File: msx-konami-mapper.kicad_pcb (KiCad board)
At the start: 2 copper layers, 65.3 x 63 mm, 1 part

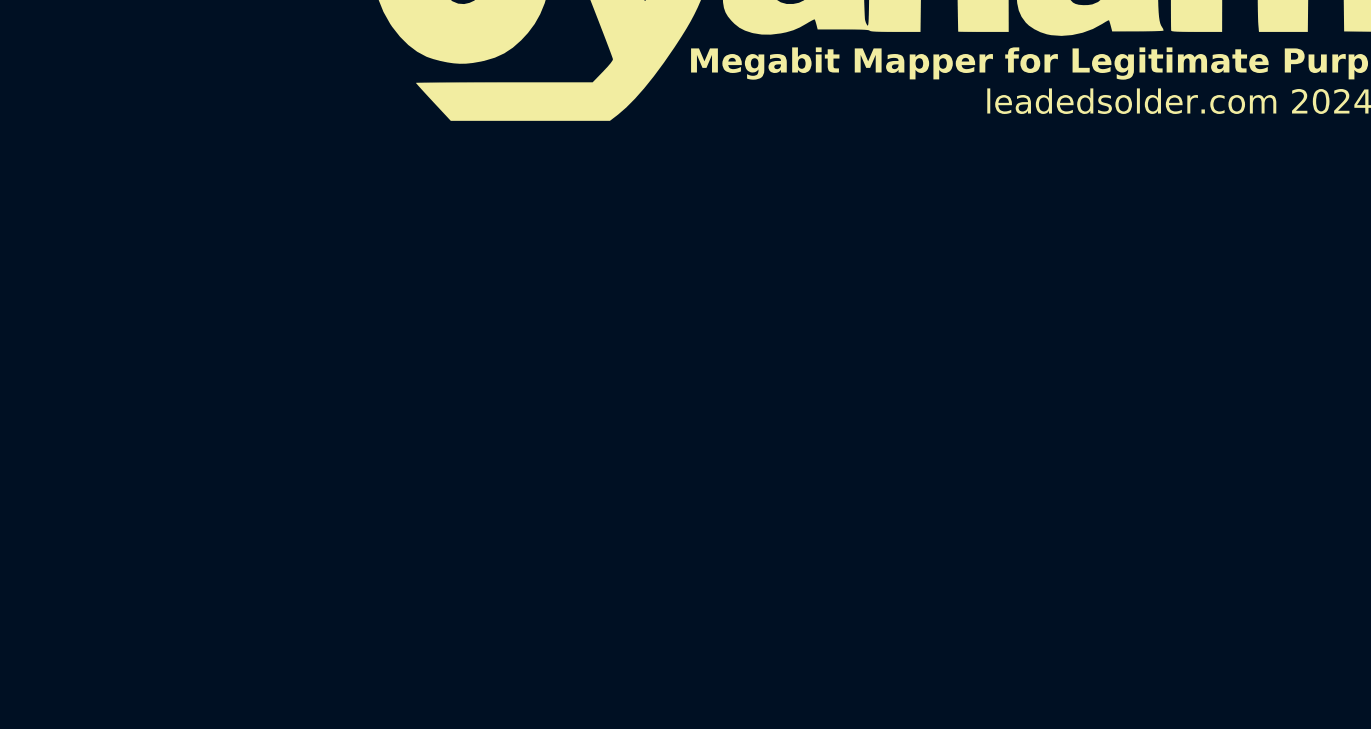
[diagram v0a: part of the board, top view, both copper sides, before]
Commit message: Placed EPROM, I may regret this
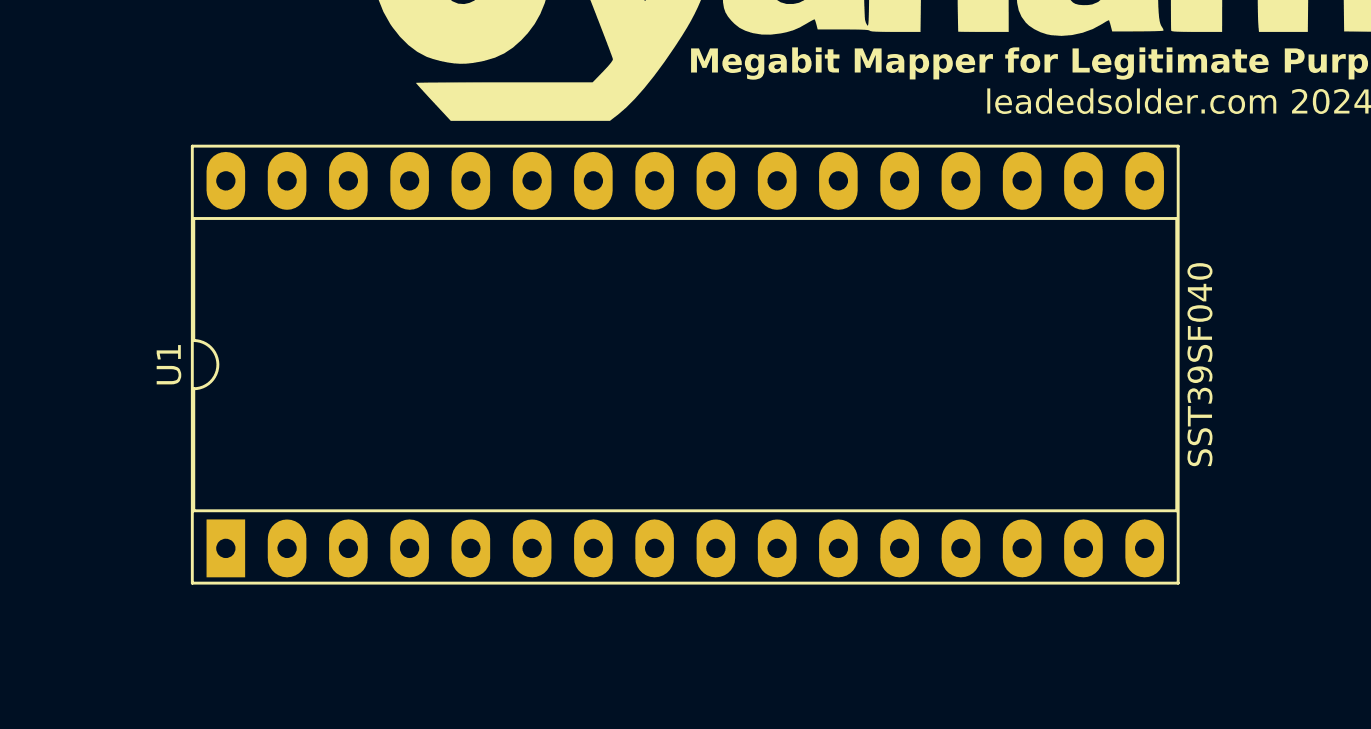
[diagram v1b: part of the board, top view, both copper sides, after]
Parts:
- added U1: SST39SF040, Package_DIP:DIP-32_W15.24mm_Socket_LongPads, F.Cu at (153.7, 80.0)

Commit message: Edge connector
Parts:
- added U2: ~, MSX:Cartridge, F.Cu at (142.2, 100.3)

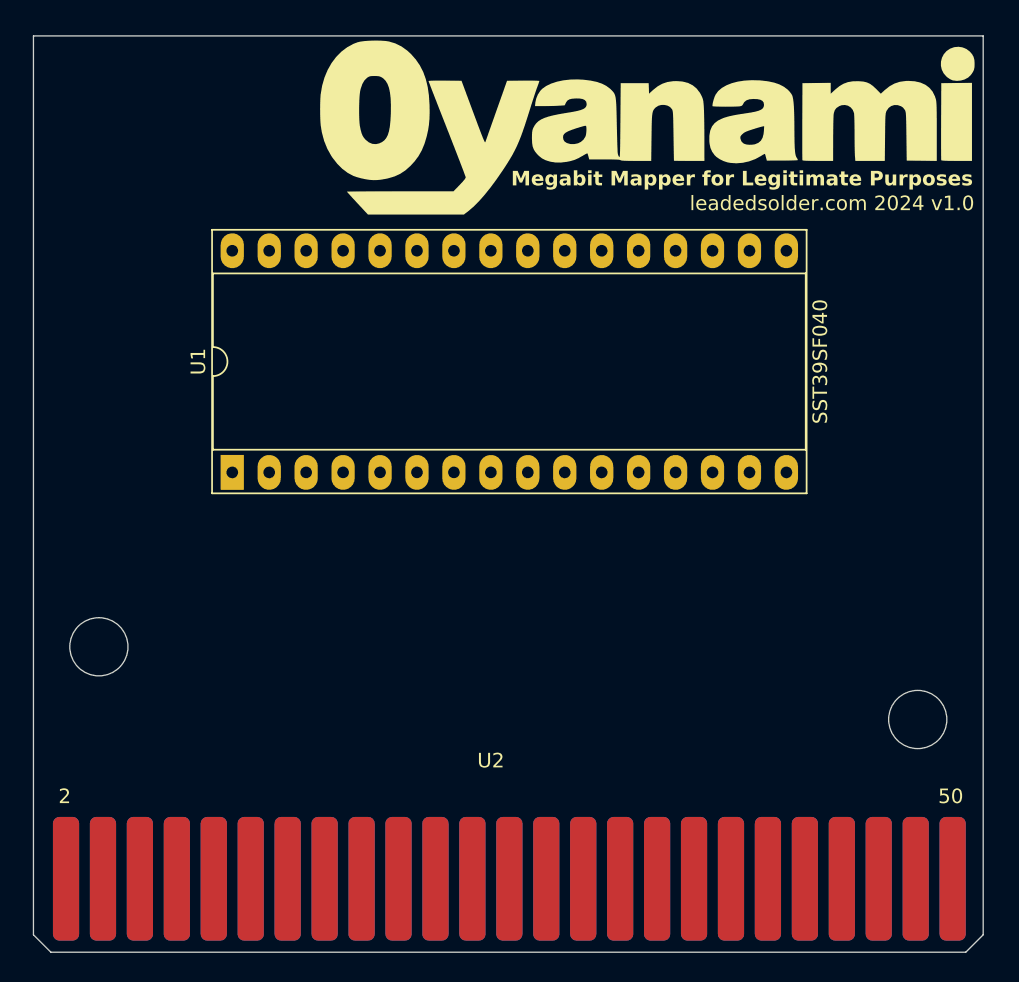
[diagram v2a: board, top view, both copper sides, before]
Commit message: Put the connector the right way around, dimwit
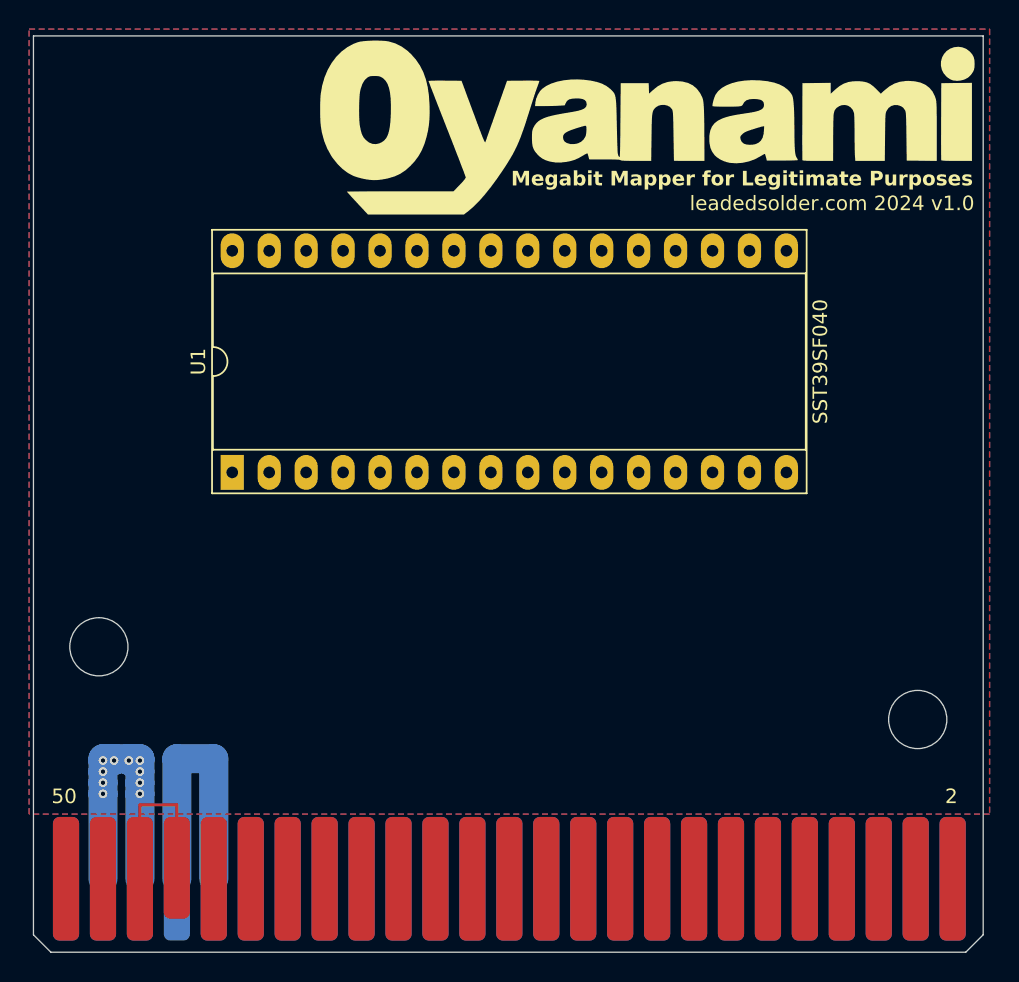
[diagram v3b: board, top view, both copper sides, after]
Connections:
- U2 pad 44: unconnected-(U2-SW1-Pad44) -> Net-(U2-SW1)
- U2 pad 46: unconnected-(U2-SW2-Pad46) -> Net-(U2-SW1)
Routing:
- net +5V: track 0.00 -> 19.3 mm, vias 0 -> 10
- net GND: track 0.00 -> 19.1 mm
- net Net-(U2-SW1): track 0.00 -> 12.0 mm
- added copper zone on F.Cu, net +5V
- added copper zone on B.Cu, net GND

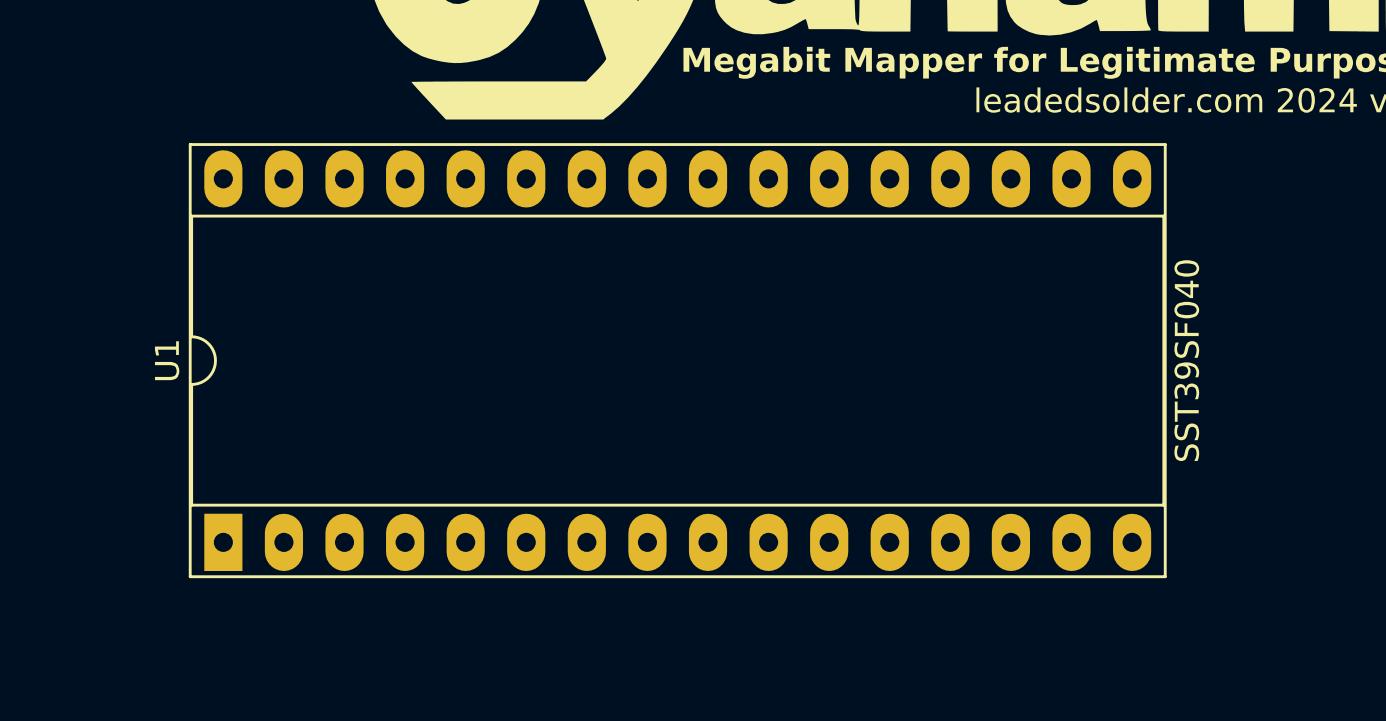
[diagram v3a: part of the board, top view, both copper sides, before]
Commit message: Data pins
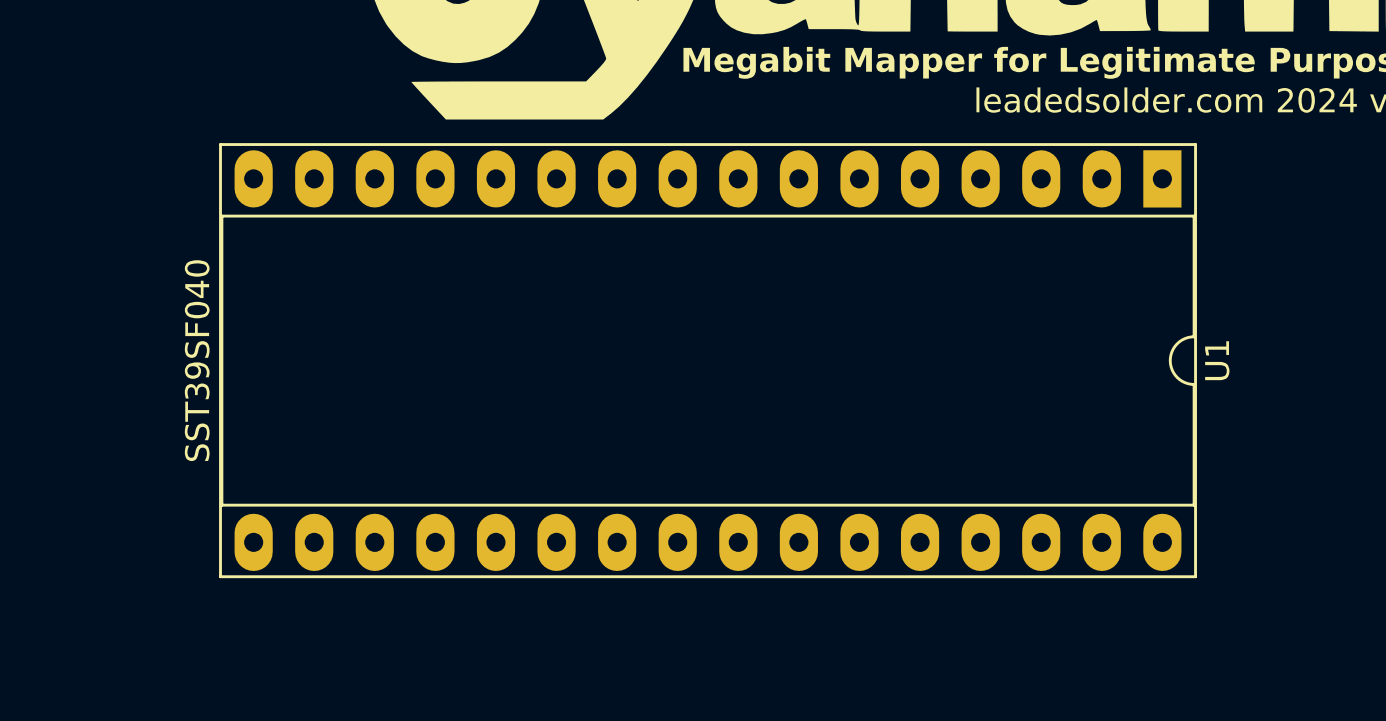
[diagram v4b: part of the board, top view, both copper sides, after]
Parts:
- moved U1 42.2 mm to (193.0, 64.8), turned to -90 degrees
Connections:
- U1 pad 13: unconnected-(U1-D0-Pad13) -> /D0
- U1 pad 14: unconnected-(U1-D1-Pad14) -> /D1
- U1 pad 15: unconnected-(U1-D2-Pad15) -> /D2
- U1 pad 16: unconnected-(U1-GND-Pad16) -> GND
- U1 pad 17: unconnected-(U1-D3-Pad17) -> /D3
- U1 pad 18: unconnected-(U1-D4-Pad18) -> /D4
- U1 pad 19: unconnected-(U1-D5-Pad19) -> /D5
- U1 pad 20: unconnected-(U1-D6-Pad20) -> /D6
- U1 pad 21: unconnected-(U1-D7-Pad21) -> /D7
- U1 pad 32: unconnected-(U1-VCC-Pad32) -> +5V
- U2 pad 33: unconnected-(U2-D1-Pad33) -> /D1
- U2 pad 34: unconnected-(U2-D0-Pad34) -> /D0
- U2 pad 35: unconnected-(U2-D3-Pad35) -> /D3
- U2 pad 36: unconnected-(U2-D2-Pad36) -> /D2
- U2 pad 37: unconnected-(U2-D5-Pad37) -> /D5
- U2 pad 38: unconnected-(U2-D4-Pad38) -> /D4
- U2 pad 39: unconnected-(U2-D7-Pad39) -> /D7
- U2 pad 40: unconnected-(U2-D6-Pad40) -> /D6

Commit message: Super gross data bus I'll probably tear up later
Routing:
- net /D2: track 0.00 -> 52.6 mm, vias 0 -> 5
- net /D0: track 0.00 -> 50.1 mm, vias 0 -> 5
- net /D1: track 0.00 -> 45.0 mm, vias 0 -> 2
- net /D7: track 0.00 -> 38.1 mm, vias 0 -> 2
- net /D6: track 0.00 -> 34.8 mm, vias 0 -> 3
- net /D3: track 0.00 -> 33.9 mm, vias 0 -> 2
- net /D5: track 0.00 -> 30.5 mm, vias 0 -> 2
- net /D4: track 0.00 -> 29.0 mm, vias 0 -> 1

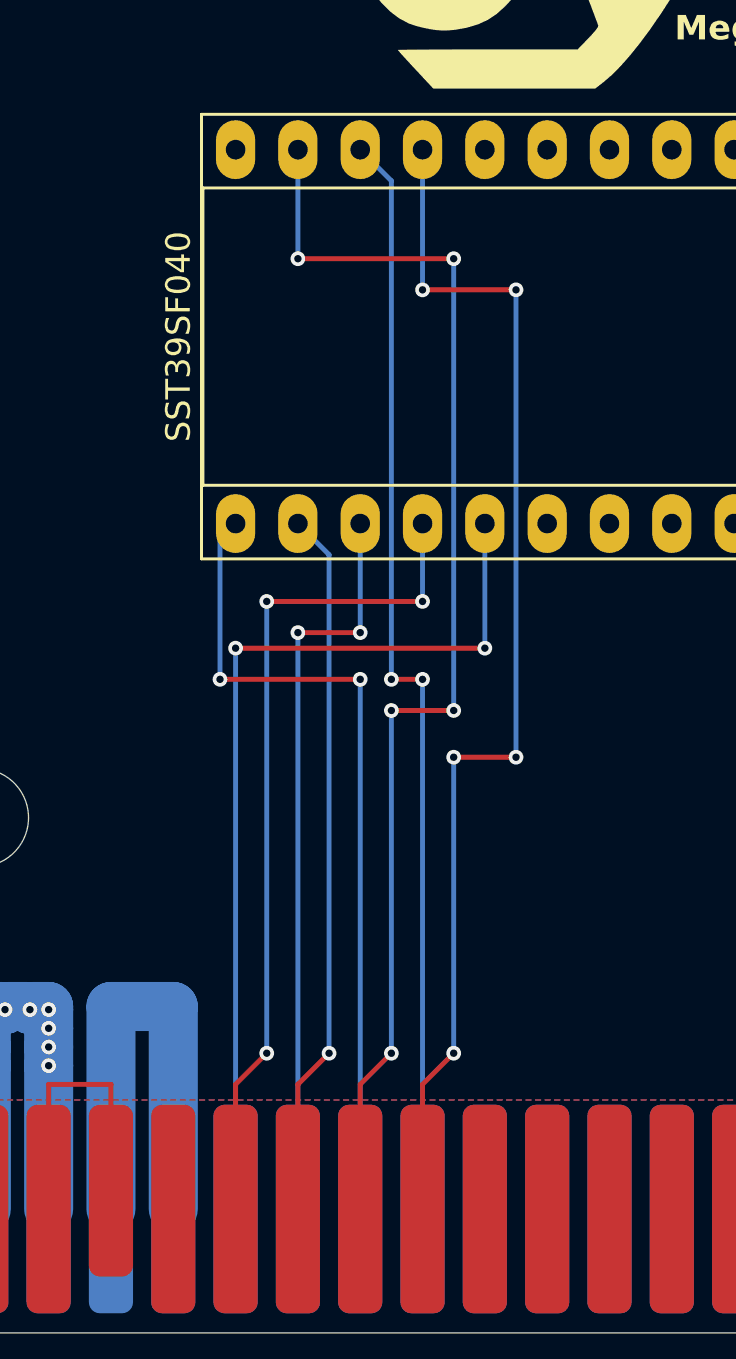
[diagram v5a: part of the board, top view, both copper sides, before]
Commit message: Wipe the data bus after all
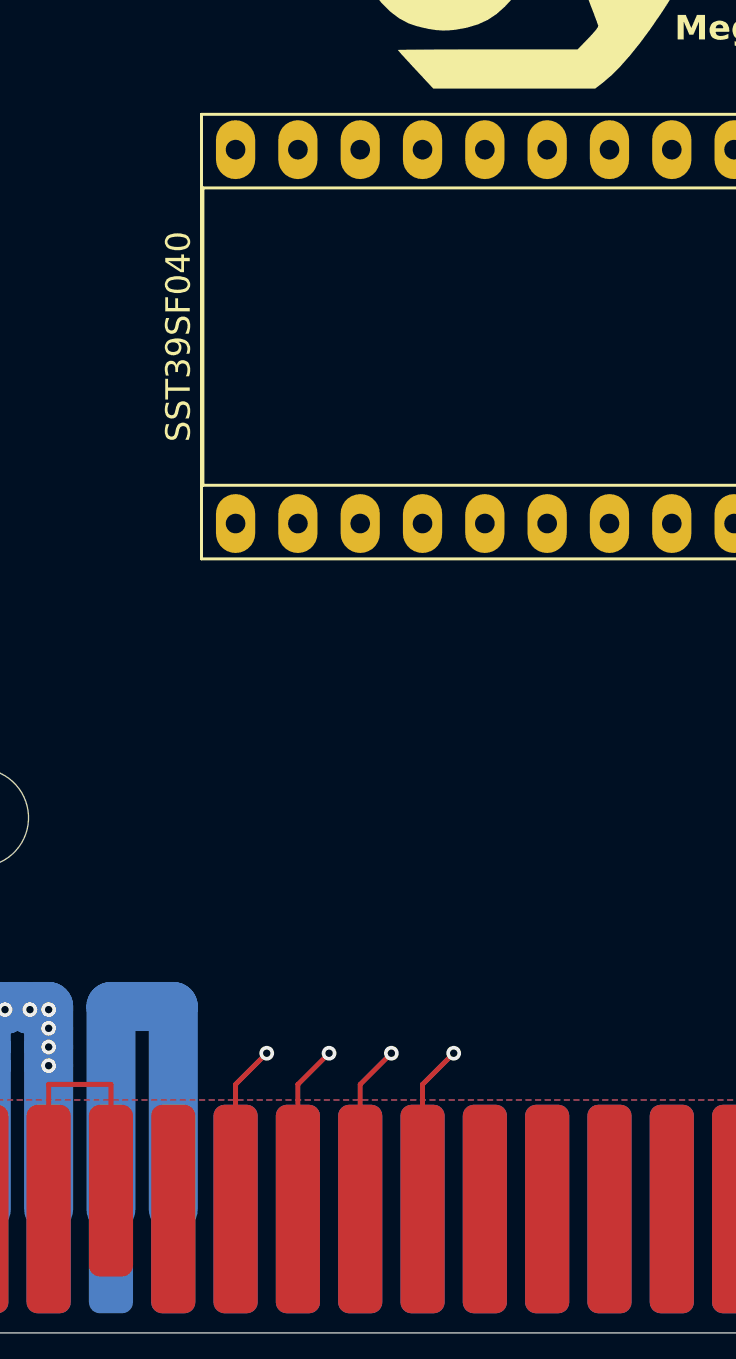
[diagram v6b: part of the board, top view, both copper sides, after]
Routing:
- net /D2: track 52.6 -> 6.88 mm, vias 5 -> 1
- net /D1: track 45.0 -> 0.00 mm, vias 2 -> 0
- net /D0: track 50.1 -> 6.88 mm, vias 5 -> 1
- net /D7: track 38.1 -> 0.00 mm, vias 2 -> 0
- net /D3: track 33.9 -> 0.90 mm, vias 2 -> 0
- net /D5: track 30.5 -> 0.00 mm, vias 2 -> 0
- net /D6: track 34.8 -> 6.88 mm, vias 3 -> 1
- net /D4: track 29.0 -> 6.88 mm
